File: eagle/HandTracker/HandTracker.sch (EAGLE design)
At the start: 22 parts, among them J1 ZX62-AB-5PA(31), U1 LSM9DS1TR, U2 MAX11629EEE+21-0055_E16+5_MXM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

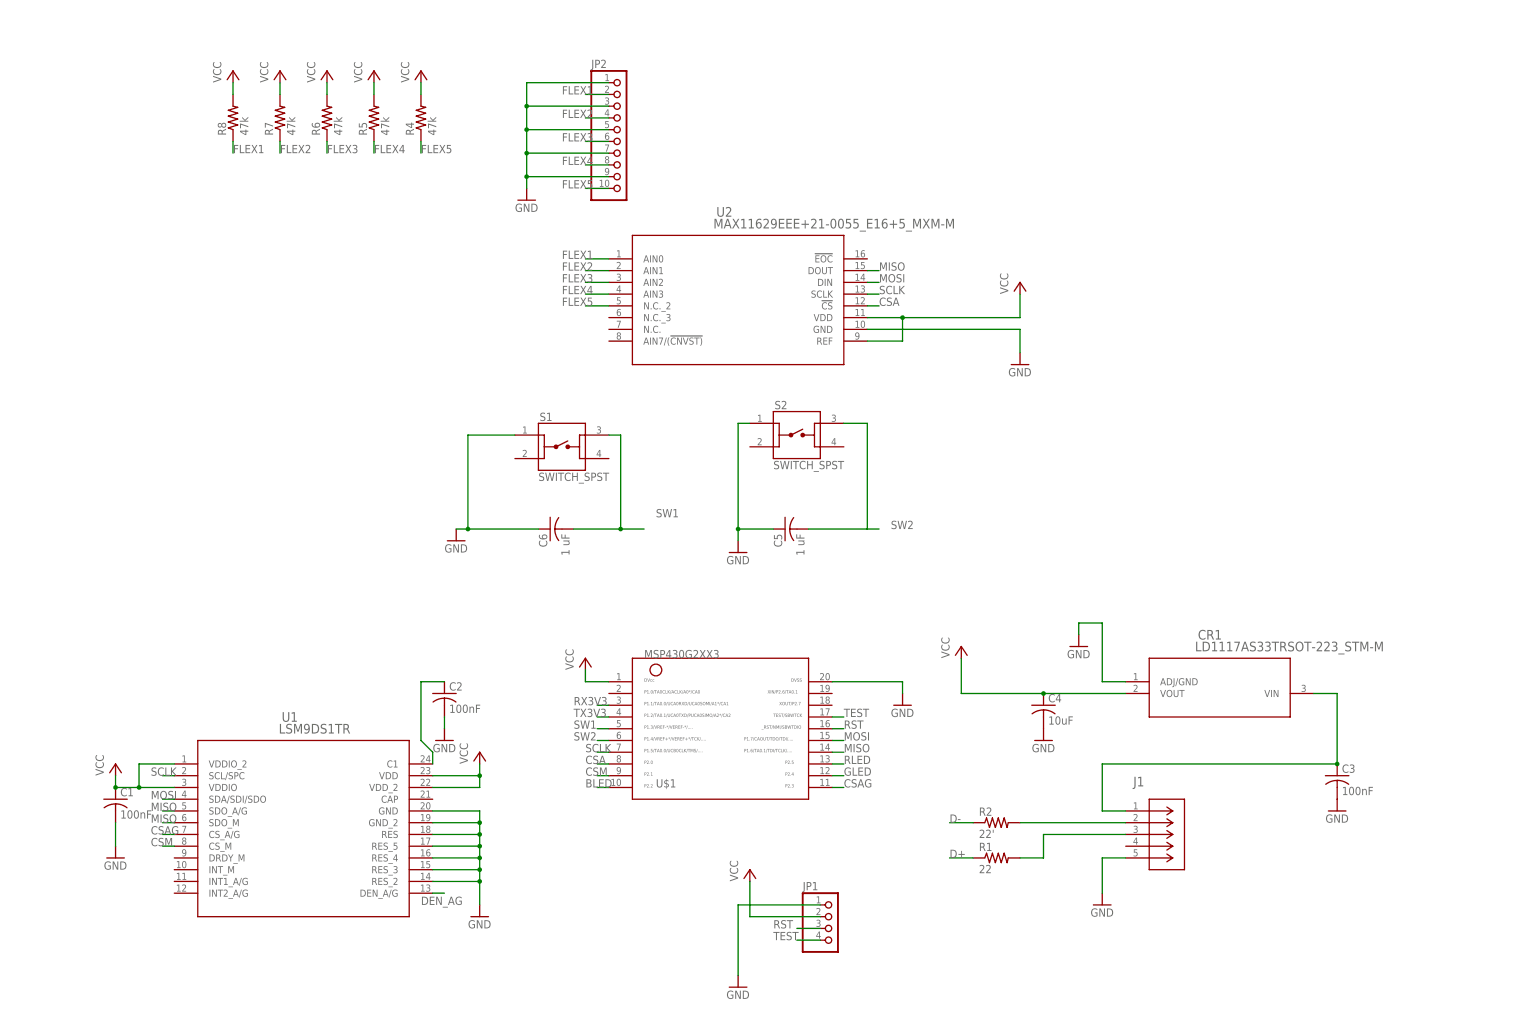
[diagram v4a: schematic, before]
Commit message: added FT232RL, still need to add LED
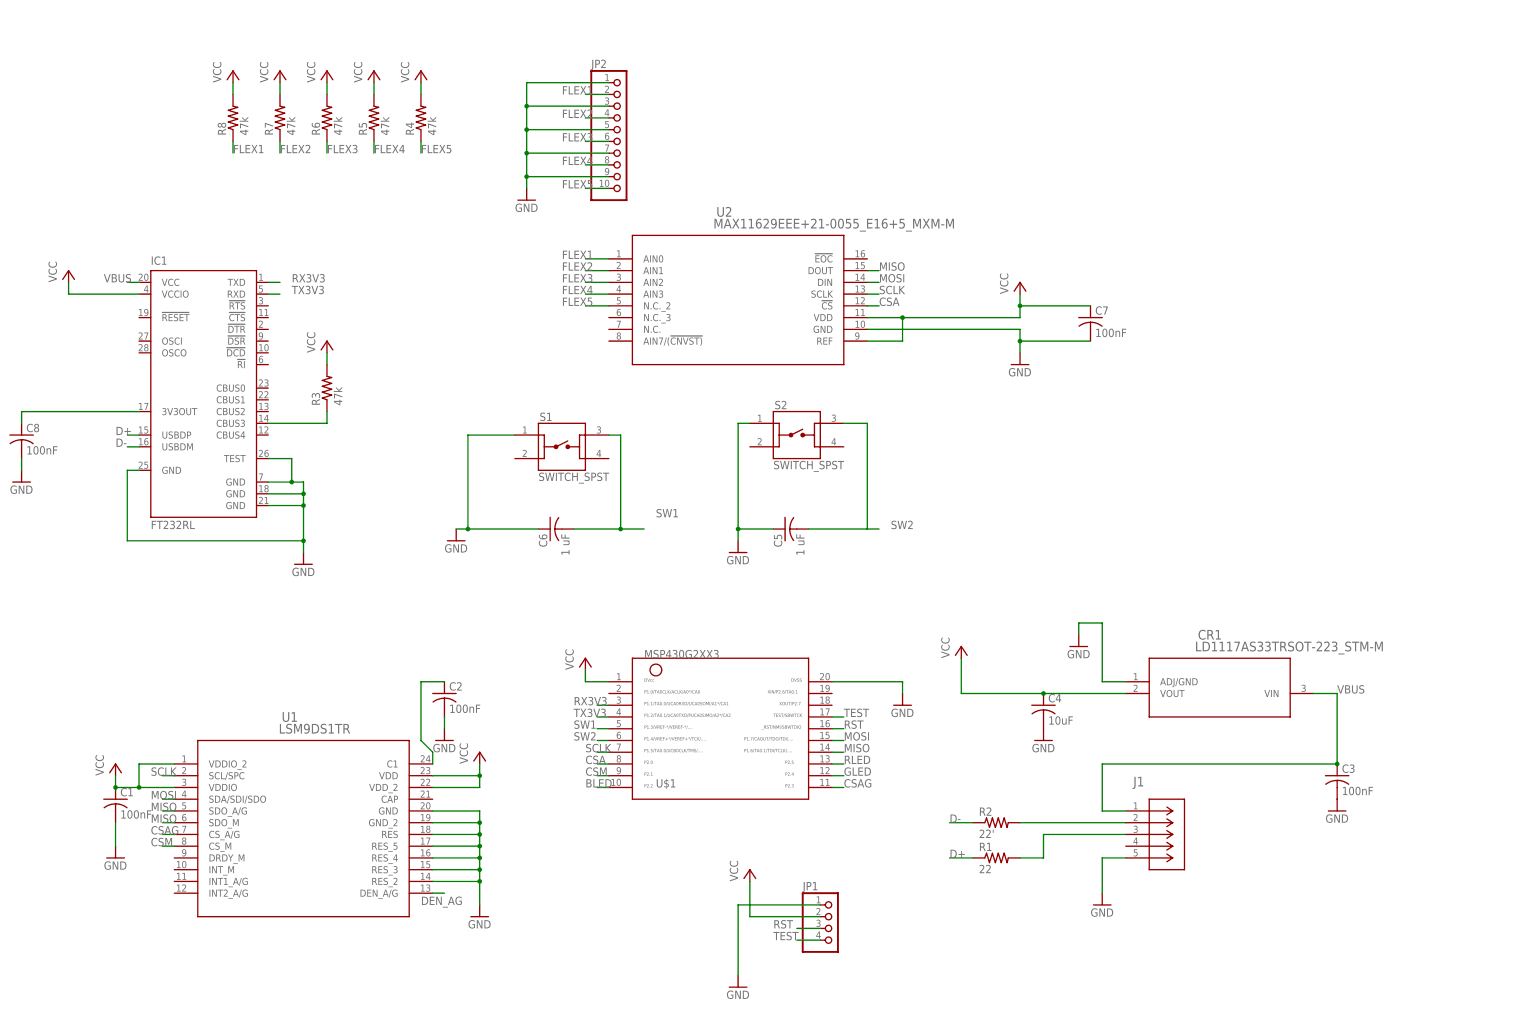
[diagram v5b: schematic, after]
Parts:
- added C7, C8: 100nF, rcl:C-USC1206
- added IC1: FT232RL, ftdichip:FT232RL
- added R3: 47k, rcl:R-US_R1206
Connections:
- new net N$4: IC1.CBUS3, R3.1
- new net VBUS: C3.1, CR1.VIN, IC1.VCC, J1.VCC
- net D+: now also IC1.USBDP
- net D-: now also IC1.USBDM
- net GND: now also C7.2, C8.2, IC1.GND, IC1.GND@1, IC1.GND@2, IC1.GND@A, IC1.TEST
- net N$3: now also C8.1, IC1.3V3OUT; no longer C3.1, CR1.VIN, J1.VCC
- net RX3V3: now also IC1.TXD
- net TX3V3: now also IC1.RXD
- net VCC: now also C7.1, IC1.VCCIO, R3.2
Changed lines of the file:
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@@
 <part name="C5" library="rcl" library_urn="urn:adsk.eagle:library:334" deviceset="C-US" device="C1206" package3d_urn="urn:adsk.eagle:package:23618/2" value="1 uF"/>
 <part name="GND11" library="supply1" library_urn="urn:adsk.eagle:library:371" deviceset="GND" device=""/>
+<part name="C7" library="rcl" library_urn="urn:adsk.eagle:library:334" deviceset="C-US" device="C1206" package3d_urn="urn:adsk.eagle:package:23618/2" value="100nF"/>
+<part name="IC1" library="ftdichip" library_urn="urn:adsk.eagle:library:231" deviceset="FT232R" device="L" package3d_urn="urn:adsk.eagle:package:14013/1"/>
+<part name="C8" library="rcl" library_urn="urn:adsk.eagle:library:334" deviceset="C-US" device="C1206" package3d_urn="urn:adsk.eagle:package:23618/2" value="100nF"/>
+<part name="GND12" library="supply1" library_urn="urn:adsk.eagle:library:371" deviceset="GND" device=""/>
+<part name="GND13" library="supply1" library_urn="urn:adsk.eagle:library:371" deviceset="GND" device=""/>
+<part name="P+7" library="supply1" library_urn="urn:adsk.eagle:library:371" deviceset="VCC" device=""/>
+<part name="R3" library="rcl" library_urn="urn:adsk.eagle:library:334" deviceset="R-US_" device="R1206" package3d_urn="urn:adsk.eagle:package:23540/2" value="47k"/>
+<part name="P+13" library="supply1" library_urn="urn:adsk.eagle:library:371" deviceset="VCC" device=""/>
 </parts>
 <sheets>
@@
 <attribute name="VALUE" x="55.88" y="15.24" size="1.778" layer="96"/>
 </instance>
+<instance part="C7" gate="G$1" x="134.62" y="68.58" smashed="yes">
+<attribute name="NAME" x="135.636" y="69.215" size="1.778" layer="95"/>
+<attribute name="VALUE" x="135.636" y="64.389" size="1.778" layer="96"/>
+</instance>
+<instance part="IC1" gate="1" x="-58.42" y="53.34" smashed="yes">
+<attribute name="NAME" x="-68.58" y="80.01" size="1.778" layer="95"/>
+<attribute name="VALUE" x="-68.58" y="22.86" size="1.778" layer="96"/>
+</instance>
+<instance part="C8" gate="G$1" x="-96.52" y="43.18" smashed="yes">
+<attribute name="NAME" x="-95.504" y="43.815" size="1.778" layer="95"/>
+<attribute name="VALUE" x="-95.504" y="38.989" size="1.778" layer="96"/>
+</instance>
+<instance part="GND12" gate="1" x="-96.52" y="33.02" smashed="yes">
+<attribute name="VALUE" x="-99.06" y="30.48" size="1.778" layer="96"/>
+</instance>
+<instance part="GND13" gate="1" x="-35.56" y="15.24" smashed="yes">
+<attribute name="VALUE" x="-38.1" y="12.7" size="1.778" layer="96"/>
+</instance>
+<instance part="P+7" gate="VCC" x="-86.36" y="78.74" smashed="yes">
+<attribute name="VALUE" x="-88.9" y="76.2" size="1.778" layer="96" rot="R90"/>
+</instance>
+<instance part="R3" gate="G$1" x="-30.48" y="53.34" smashed="yes" rot="R90">
+<attribute name="NAME" x="-31.9786" y="49.53" size="1.778" layer="95" rot="R90"/>
+<attribute name="VALUE" x="-27.178" y="49.53" size="1.778" layer="96" rot="R90"/>
+</instance>
+<instance part="P+13" gate="VCC" x="-30.48" y="63.5" smashed="yes">
+<attribute name="VALUE" x="-33.02" y="60.96" size="1.778" layer="96" rot="R90"/>
+</instance>
 </instances>
 <busses>
@@
 <pinref part="U2" gate="A" pin="GND"/>
 <wire x1="86.36" y1="66.04" x2="119.38" y2="66.04" width="0.1524" layer="91"/>
-<wire x1="119.38" y1="66.04" x2="119.38" y2="60.96" width="0.1524" layer="91"/>
+<wire x1="119.38" y1="66.04" x2="119.38" y2="63.5" width="0.1524" layer="91"/>
 <pinref part="GND5" gate="1" pin="GND"/>
+<pinref part="C7" gate="G$1" pin="2"/>
+<wire x1="119.38" y1="63.5" x2="119.38" y2="60.96" width="0.1524" layer="91"/>
+<wire x1="134.62" y1="63.5" x2="119.38" y2="63.5" width="0.1524" layer="91"/>
+<junction x="119.38" y="63.5"/>
 </segment>
 <segment>
@@
 <junction x="58.42" y="22.86"/>
 </segment>
-</net>
-<net name="N$3" class="0">
+<segment>
+<pinref part="C8" gate="G$1" pin="2"/>
+<pinref part="GND12" gate="1" pin="GND"/>
+<wire x1="-96.52" y1="35.56" x2="-96.52" y2="38.1" width="0.1524" layer="91"/>
+</segment>
+<segment>
+<pinref part="IC1" gate="1" pin="GND"/>
+<wire x1="-43.18" y1="33.02" x2="-38.1" y2="33.02" width="0.1524" layer="91"/>
+<pinref part="GND13" gate="1" pin="GND"/>
+<wire x1="-38.1" y1="33.02" x2="-35.56" y2="33.02" width="0.1524" layer="91"/>
+<wire x1="-35.56" y1="33.02" x2="-35.56" y2="30.48" width="0.1524" layer="91"/>
+<pinref part="IC1" gate="1" pin="GND@2"/>
+<wire x1="-35.56" y1="30.48" x2="-35.56" y2="27.94" width="0.1524" layer="91"/>
+<wire x1="-35.56" y1="27.94" x2="-35.56" y2="20.32" width="0.1524" layer="91"/>
+<wire x1="-35.56" y1="20.32" x2="-35.56" y2="17.78" width="0.1524" layer="91"/>
+<wire x1="-43.18" y1="27.94" x2="-35.56" y2="27.94" width="0.1524" layer="91"/>
+<junction x="-35.56" y="27.94"/>
+<pinref part="IC1" gate="1" pin="GND@1"/>
+<wire x1="-43.18" y1="30.48" x2="-35.56" y2="30.48" width="0.1524" layer="91"/>
+<junction x="-35.56" y="30.48"/>
+<pinref part="IC1" gate="1" pin="GND@A"/>
+<wire x1="-71.12" y1="35.56" x2="-73.66" y2="35.56" width="0.1524" layer="91"/>
+<wire x1="-73.66" y1="35.56" x2="-73.66" y2="20.32" width="0.1524" layer="91"/>
+<wire x1="-73.66" y1="20.32" x2="-35.56" y2="20.32" width="0.1524" layer="91"/>
+<junction x="-35.56" y="20.32"/>
+<pinref part="IC1" gate="1" pin="TEST"/>
+<wire x1="-43.18" y1="38.1" x2="-38.1" y2="38.1" width="0.1524" layer="91"/>
+<wire x1="-38.1" y1="38.1" x2="-38.1" y2="33.02" width="0.1524" layer="91"/>
+<junction x="-38.1" y="33.02"/>
+</segment>
+</net>
+<net name="VBUS" class="0">
 <segment>
 <pinref part="J1" gate="A" pin="VCC"/>
@@
 <pinref part="C3" gate="G$1" pin="1"/>
 <junction x="187.96" y="-27.94"/>
+<label x="187.96" y="-12.7" size="1.778" layer="95"/>
+</segment>
+<segment>
+<pinref part="IC1" gate="1" pin="VCC"/>
+<wire x1="-71.12" y1="76.2" x2="-73.66" y2="76.2" width="0.1524" layer="91"/>
+<label x="-78.74" y="76.2" size="1.778" layer="95"/>
 </segment>
 </net>
@@
 <wire x1="86.36" y1="68.58" x2="93.98" y2="68.58" width="0.1524" layer="91"/>
 <wire x1="93.98" y1="68.58" x2="119.38" y2="68.58" width="0.1524" layer="91"/>
-<wire x1="119.38" y1="68.58" x2="119.38" y2="73.66" width="0.1524" layer="91"/>
+<wire x1="119.38" y1="68.58" x2="119.38" y2="71.12" width="0.1524" layer="91"/>
+<wire x1="119.38" y1="71.12" x2="119.38" y2="73.66" width="0.1524" layer="91"/>
 <wire x1="93.98" y1="68.58" x2="93.98" y2="63.5" width="0.1524" layer="91"/>
 <junction x="93.98" y="68.58"/>
@@
 <wire x1="93.98" y1="63.5" x2="86.36" y2="63.5" width="0.1524" layer="91"/>
 <pinref part="P+4" gate="VCC" pin="VCC"/>
+<pinref part="C7" gate="G$1" pin="1"/>
+<wire x1="134.62" y1="71.12" x2="119.38" y2="71.12" width="0.1524" layer="91"/>
+<junction x="119.38" y="71.12"/>
 </segment>
 <segment>
@@
 <wire x1="-10.16" y1="119.38" x2="-10.16" y2="116.84" width="0.1524" layer="91"/>
 </segment>
+<segment>
+<pinref part="IC1" gate="1" pin="VCCIO"/>
+<wire x1="-71.12" y1="73.66" x2="-86.36" y2="73.66" width="0.1524" layer="91"/>
+<wire x1="-86.36" y1="73.66" x2="-86.36" y2="76.2" width="0.1524" layer="91"/>
+<pinref part="P+7" gate="VCC" pin="VCC"/>
+</segment>
+<segment>
+<pinref part="R3" gate="G$1" pin="2"/>
+<pinref part="P+13" gate="VCC" pin="VCC"/>
+<wire x1="-30.48" y1="60.96" x2="-30.48" y2="58.42" width="0.1524" layer="91"/>
+</segment>
 </net>
 <net name="D-" class="0">
@@
 <label x="104.14" y="-40.64" size="1.778" layer="95"/>
 </segment>
+<segment>
+<pinref part="IC1" gate="1" pin="USBDM"/>
+<wire x1="-71.12" y1="40.64" x2="-73.66" y2="40.64" width="0.1524" layer="91"/>
+<label x="-76.2" y="40.64" size="1.778" layer="95"/>
+</segment>
 </net>
 <net name="D+" class="0">
@@
 <label x="104.14" y="-48.26" size="1.778" layer="95"/>
 </segment>
+<segment>
+<pinref part="IC1" gate="1" pin="USBDP"/>
+<wire x1="-71.12" y1="43.18" x2="-73.66" y2="43.18" width="0.1524" layer="91"/>
+<label x="-76.2" y="43.18" size="1.778" layer="95"/>
+</segment>
 </net>
 <net name="RST" class="0">
@@
 <label x="22.86" y="-15.24" size="1.778" layer="95"/>
 </segment>
+<segment>
+<pinref part="IC1" gate="1" pin="TXD"/>
+<wire x1="-43.18" y1="76.2" x2="-40.64" y2="76.2" width="0.1524" layer="91"/>
+<label x="-38.1" y="76.2" size="1.778" layer="95"/>
+</segment>
 </net>
 <net name="TX3V3" class="0">
@@
 <wire x1="30.48" y1="-17.78" x2="27.94" y2="-17.78" width="0.1524" layer="91"/>
 <label x="22.86" y="-17.78" size="1.778" layer="95"/>
+</segment>
+<segment>
+<pinref part="IC1" gate="1" pin="RXD"/>
+<wire x1="-43.18" y1="73.66" x2="-40.64" y2="73.66" width="0.1524" layer="91"/>
+<label x="-38.1" y="73.66" size="1.778" layer="95"/>
 </segment>
 </net>
@@
 </segment>
 </net>
+<net name="N$3" class="0">
+<segment>
+<pinref part="IC1" gate="1" pin="3V3OUT"/>
+<wire x1="-71.12" y1="48.26" x2="-96.52" y2="48.26" width="0.1524" layer="91"/>
+<pinref part="C8" gate="G$1" pin="1"/>
+<wire x1="-96.52" y1="48.26" x2="-96.52" y2="45.72" width="0.1524" layer="91"/>
+</segment>
+</net>
+<net name="N$4" class="0">
+<segment>
+<pinref part="IC1" gate="1" pin="CBUS3"/>
+<wire x1="-43.18" y1="45.72" x2="-30.48" y2="45.72" width="0.1524" layer="91"/>
+<wire x1="-30.48" y1="45.72" x2="-30.48" y2="48.26" width="0.1524" layer="91"/>
+<pinref part="R3" gate="G$1" pin="1"/>
+</segment>
+</net>
